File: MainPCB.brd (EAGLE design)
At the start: 165.1 x 114.3 mm, 38 parts, among them J2 DCJ0202

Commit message: yayyy pinsssss
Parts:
- added C12, C13: 10pF, SparkFun-Capacitors:0805
- added D1: GREEN-0603, Seeed-LED:LED-0603
- added D2: BLUE-0603, Seeed-LED:LED-0603
- added H5, H6, H7, H8: STAND-OFF, SparkFun-Hardware:STAND-OFF
- added R10, R11: 100, SparkFun-Resistors:0603
- added X1: 8MHz, IQD-Frequency-Products:HC49
- moved U$7 172.0 mm to (-26.2, 6.98), turned to 180 degrees
- moved JP2 158.2 mm to (3.47, 72.5)
- moved C3 144.7 mm to (17.5, 93.8), turned to 90 degrees
- moved J2 137.0 mm to (14.2, 104.0)
- moved U$5 118.8 mm to (28.7, 88.2), turned to 180 degrees
- moved U$3 115.1 mm to (33.0, 98.2), turned to 90 degrees
- moved U$1 107.7 mm to (33.8, 58.5), turned to 270 degrees
- moved JP1 104.5 mm to (141.2, 5.54), turned to 180 degrees
- moved R4 102.9 mm to (30.4, -18.3)
- moved C1 102.9 mm to (25.3, -31.0)
- moved C10 102.9 mm to (49.5, -18.3)
- moved C11 102.9 mm to (45.6, -18.3)
- moved C2 102.9 mm to (21.5, -31.0)
- moved C5 102.9 mm to (12.6, -22.1)
- moved C6 102.9 mm to (8.81, -22.1)
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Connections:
- new net BUTT_DOWN: U$1.35
- new net BUTT_SEL: U$1.33
- new net BUTT_UP: U$1.34
- new net COLOUT_1: U$1.51
- new net COLOUT_2: U$1.52
- new net COLOUT_3: U$1.53
- new net COLOUT_4: U$1.54
- new net COLOUT_5: U$1.57
- new net COLOUT_6: U$1.58
- new net COLOUT_7: U$1.59
- new net COLOUT_8: U$1.61
- new net COLOUT_9: U$1.62
- new net N$1: C12.2, U$1.5, X1.1
- new net N$2: C13.1, U$1.6, X1.2
- new net N$4: R10.1, U$1.45
- new net N$5: D1.+, R10.2
- new net N$6: R11.1, U$1.44
- new net N$7: D2.+, R11.2
- net GND: now also C12.1, C13.2, D1.-, D2.-
- net MOSI: now also U$1.11; no longer U$1.36
- net RX_ESP: now also U$1.43; no longer U$1.58
- net SCLK: now also U$1.29; no longer U$1.34
- net TX_ESP: now also U$1.42; no longer U$1.59

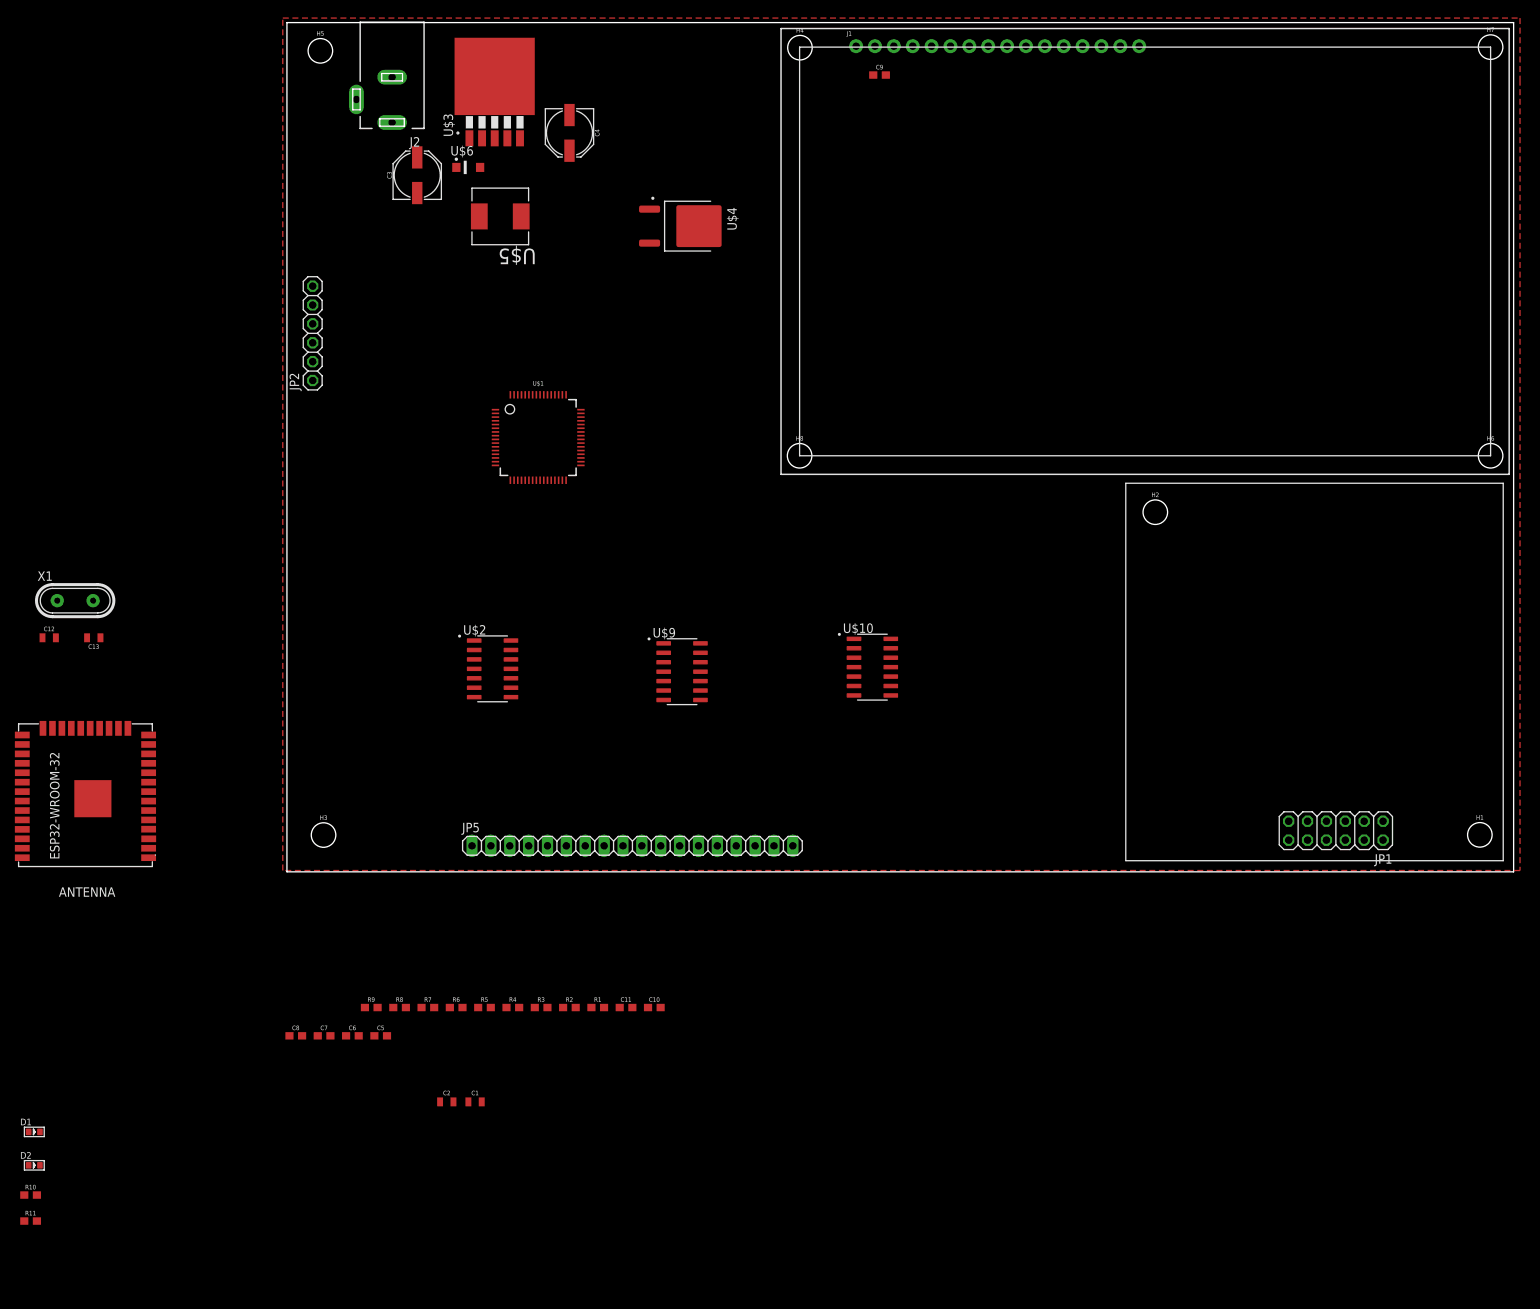
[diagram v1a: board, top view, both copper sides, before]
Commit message: added reset switch
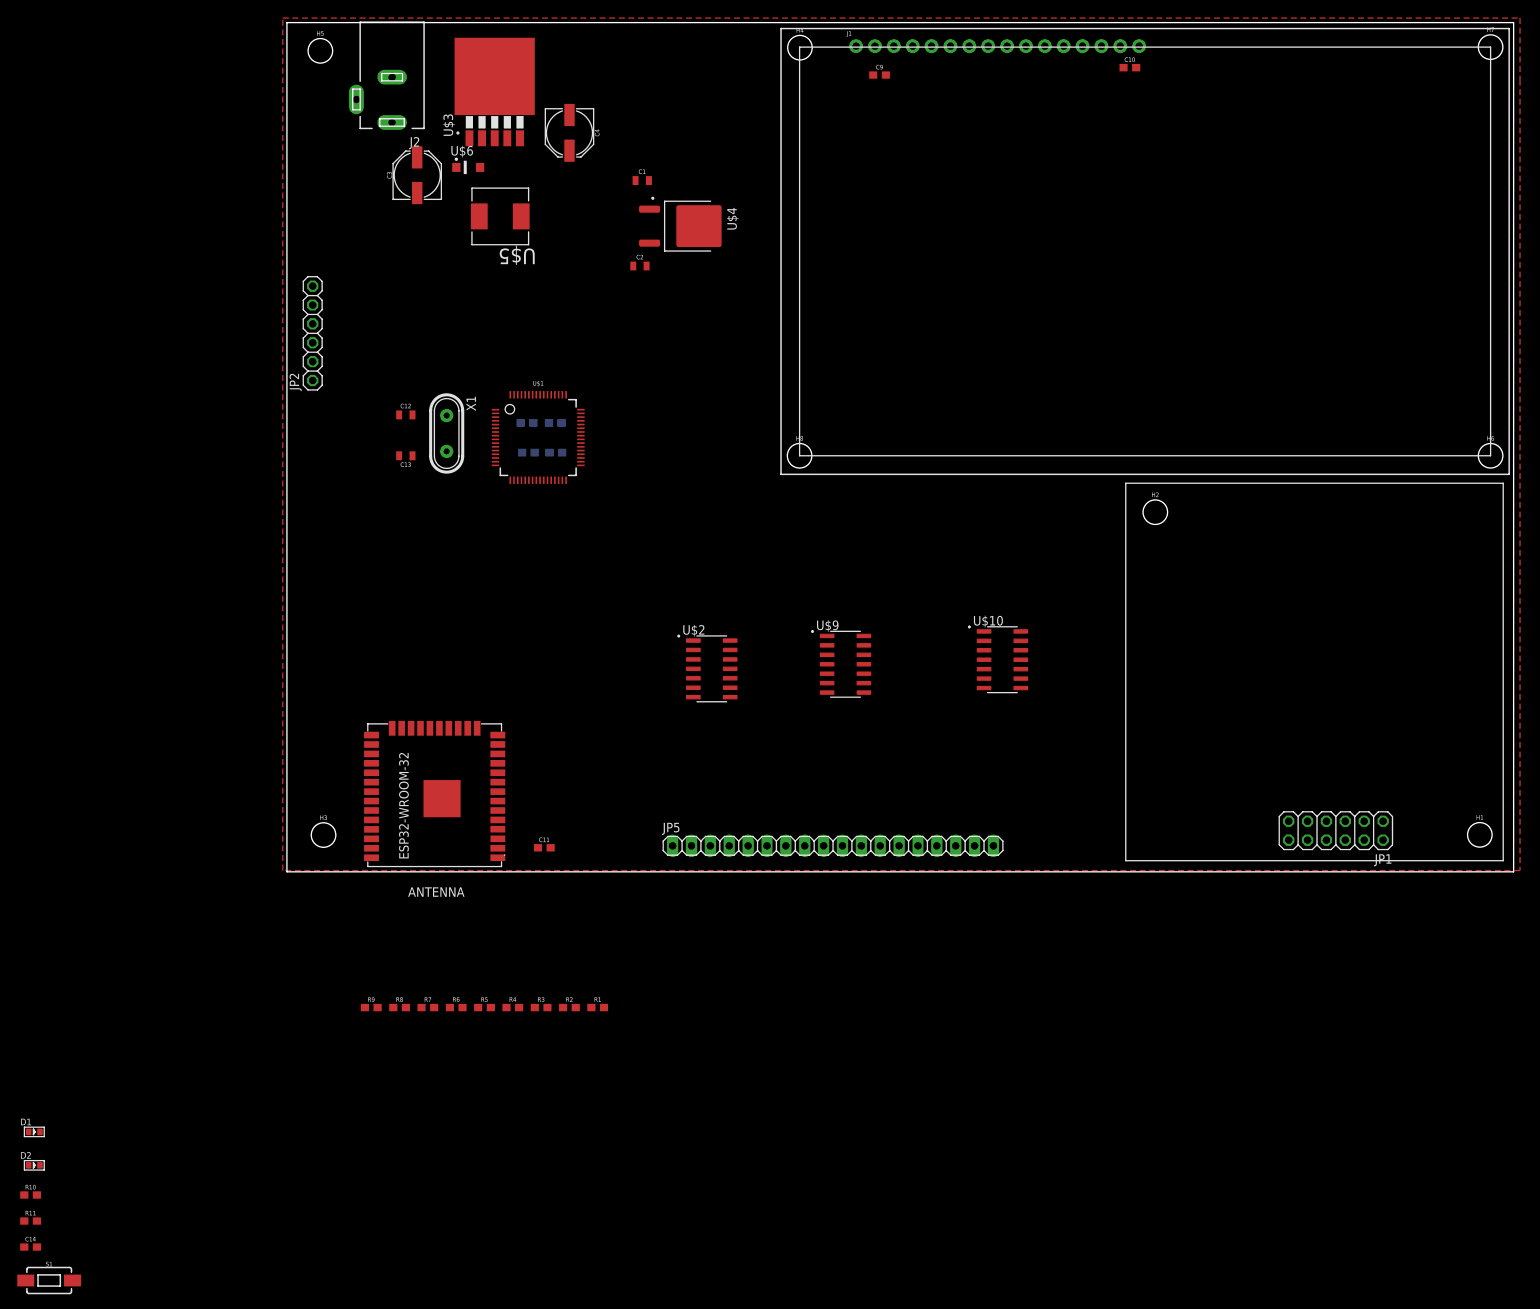
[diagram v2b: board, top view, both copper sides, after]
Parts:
- added C14: 0.1uF, SparkFun-Capacitors:0603
- added S1: MOMENTARY-SWITCH-SPST-SMD-6.0X3.5MM, SparkFun-Switches:TACTILE_SWITCH_SMD_6.0X3.5MM
- moved C10 141.8 mm to (113.5, 108.2)
- moved C1 126.0 mm to (47.8, 93.0)
- moved C2 115.5 mm to (47.5, 81.5)
- moved C8 85.9 mm to (36.2, 56.4), flipped to the bottom
- moved C5 85.8 mm to (36.1, 60.4), flipped to the bottom
- moved C6 85.8 mm to (32.3, 60.4), flipped to the bottom
- moved C7 83.2 mm to (32.5, 56.4), flipped to the bottom
- moved C12 56.6 mm to (16.0, 61.5)
- moved X1 54.8 mm to (21.5, 59.0), turned to 270 degrees
- moved C13 48.6 mm to (16.0, 56.0)
- moved U$7 47.0 mm to (20.8, 6.98)
- moved U$2 29.5 mm to (57.2, 27.3)
- moved JP5 27.0 mm to (73.5, 3.50)
- moved C11 24.2 mm to (34.6, 3.24)
- moved U$9 22.0 mm to (75.2, 27.9)
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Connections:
- net 3.3V: now also C14.1, S1.2, U$1.7
- net GND: now also C14.2, S1.1
- net NRST: no longer U$1.7

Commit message: added some pins for buttons
also changed the layout slightly
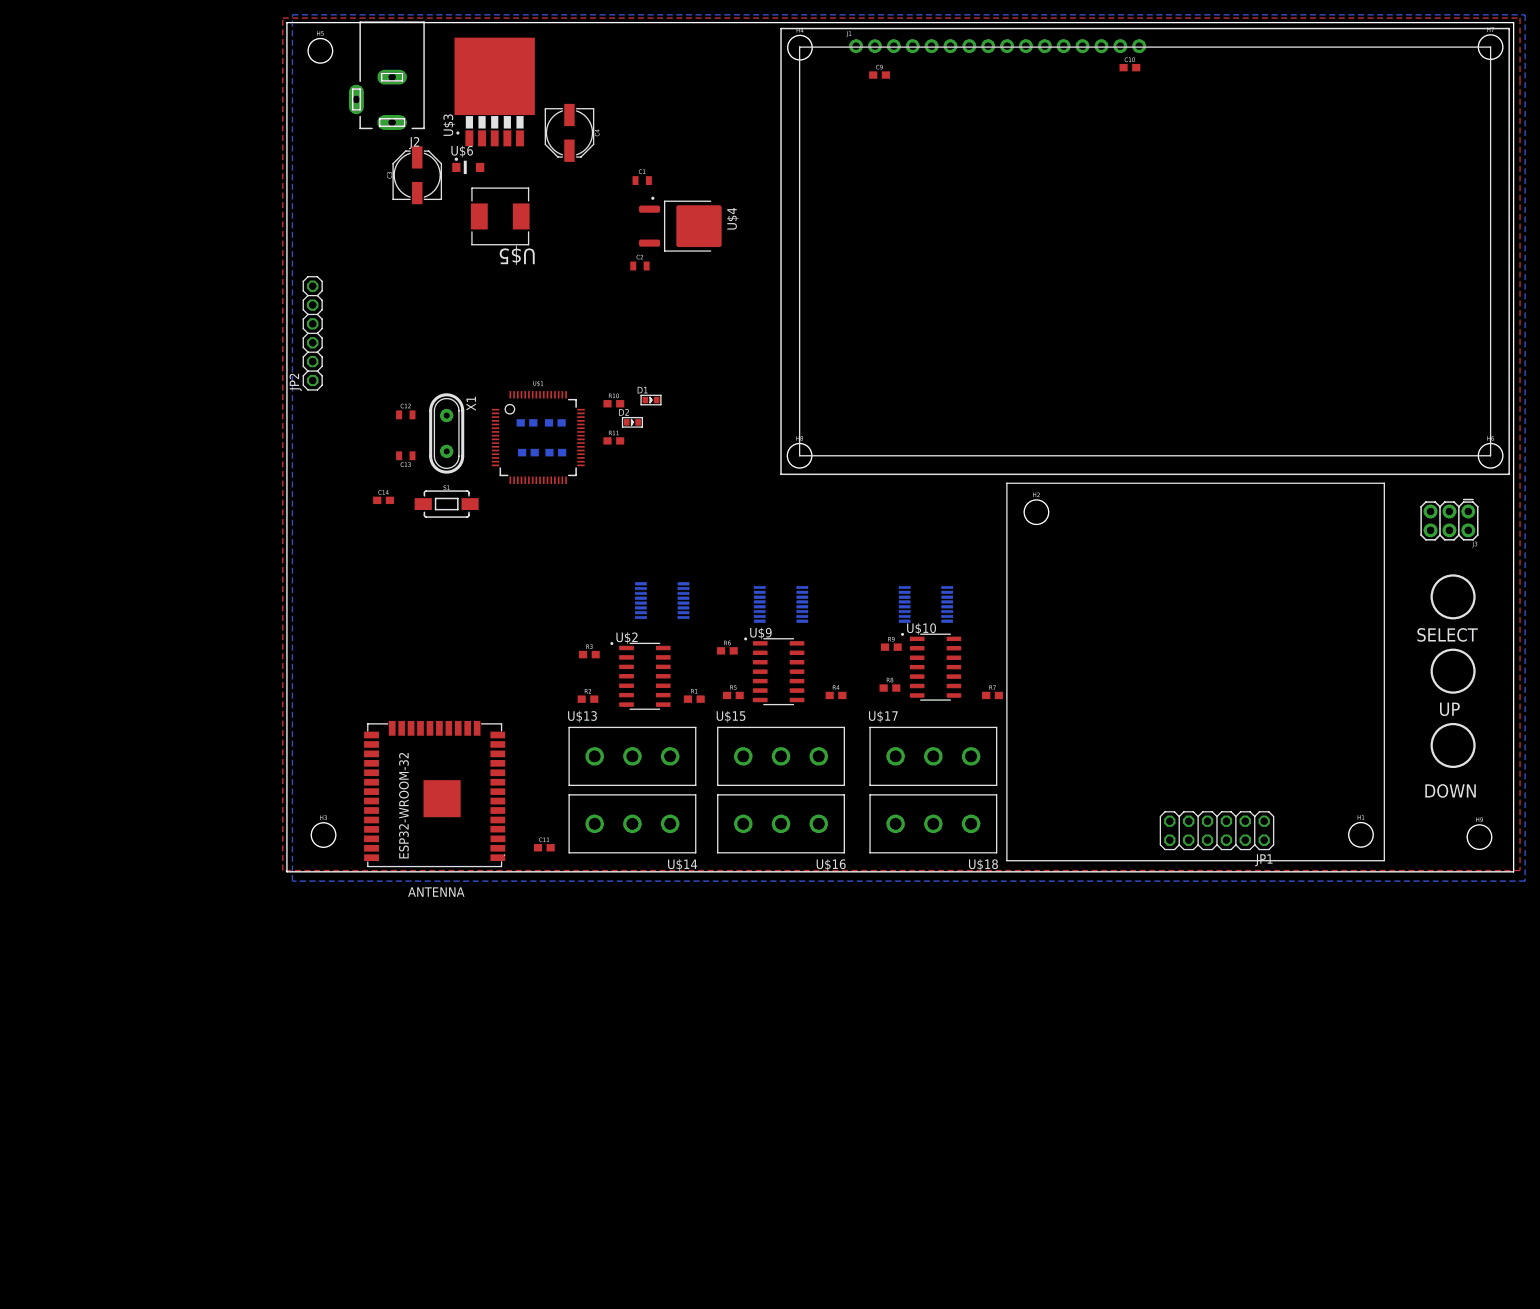
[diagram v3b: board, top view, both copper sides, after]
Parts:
- removed JP5: (no value), pinhead:1X18
- added H9: STAND-OFF, SparkFun-Hardware:STAND-OFF
- added J3: FEMALE 2x3, SparkFun-Connectors:2X3
- added U$11, U$12, U$8: TMUX1112PWR, SeniorDesignParts:16-TSSOP
- added U$13, U$14, U$15, U$16, U$17, U$18: 3PINCONN, SeniorDesignParts:3PINCONN
- moved R10 132.3 mm to (44.0, 63.0)
- moved R11 131.1 mm to (44.0, 58.0)
- moved D1 128.8 mm to (49.0, 63.5)
- moved D2 128.4 mm to (46.5, 60.5)
- moved S1 117.4 mm to (21.5, 49.5)
- moved C14 111.2 mm to (13.0, 50.0)
- moved R7 86.8 mm to (95.0, 23.7)
- moved R9 85.2 mm to (81.3, 30.2)
- moved R8 78.8 mm to (81.2, 24.7)
- moved R4 60.5 mm to (73.9, 23.7)
- moved R6 60.3 mm to (59.3, 29.7)
- moved R5 53.7 mm to (60.1, 23.7)
- moved R3 47.9 mm to (40.7, 29.2)
- moved R1 43.5 mm to (54.8, 23.2)
- moved R2 41.6 mm to (40.5, 23.2)
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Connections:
- new net COL1: U$14.A
- new net COL2: U$14.B
- new net COL3: U$14.C
- new net COL4: U$16.A
- new net COL5: U$16.B
- new net COL6: U$16.C
- new net COL7: U$18.A
- new net COL8: U$18.B
- new net COL9: U$18.C
- net BUTT_DOWN: now also J3.5
- net BUTT_SEL: now also J3.1
- net BUTT_UP: now also J3.3
- net GND: now also J3.2, J3.4, J3.6
- net ROW1: now also U$13.A; no longer JP5.1
- net ROW2: now also U$13.B; no longer JP5.2
- net ROW3: now also U$13.C; no longer JP5.3
- net ROW4: now also U$15.A; no longer JP5.4
- net ROW5: now also U$15.B; no longer JP5.5
- net ROW6: now also U$15.C; no longer JP5.6
- net ROW7: now also U$17.A; no longer JP5.7
- net ROW8: now also U$17.B; no longer JP5.8
- net ROW9: now also U$17.C; no longer JP5.9
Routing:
- added copper zone on layer 16, net GND
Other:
- board text added: "DOWN"
- board text added: "SELECT"
- board text added: "UP"

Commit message: the finer things
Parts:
- added R12, R13: 100k, SparkFun-Resistors:0603
- added R14, R15, R16: 3.3k, SparkFun-Resistors:0603
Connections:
- new net N$9: R13.2, U$1.60
- net 3.3V: now also R12.2, R14.2, R15.2, R16.2, U$1.1; no longer C14.1, S1.2, U$1.7
- net BUTT_DOWN: now also R14.1
- net BUTT_SEL: now also R16.1
- net BUTT_UP: now also R15.1
- net GND: now also R13.1, U$11.5, U$12.5, U$8.5
- net NRST: now also C14.1, R12.1, S1.2, U$1.7
